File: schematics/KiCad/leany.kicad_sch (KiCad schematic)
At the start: 23 parts, among them J1 SWD, J2 SSD1306, SW2 ZERO_BTN, SW3 HOLD_BTN, SW4 BOOTMODE_SW, U1 STM32F103C8Tx, U3 LSM6DSO, U4 CH340C, Y1 8MHz

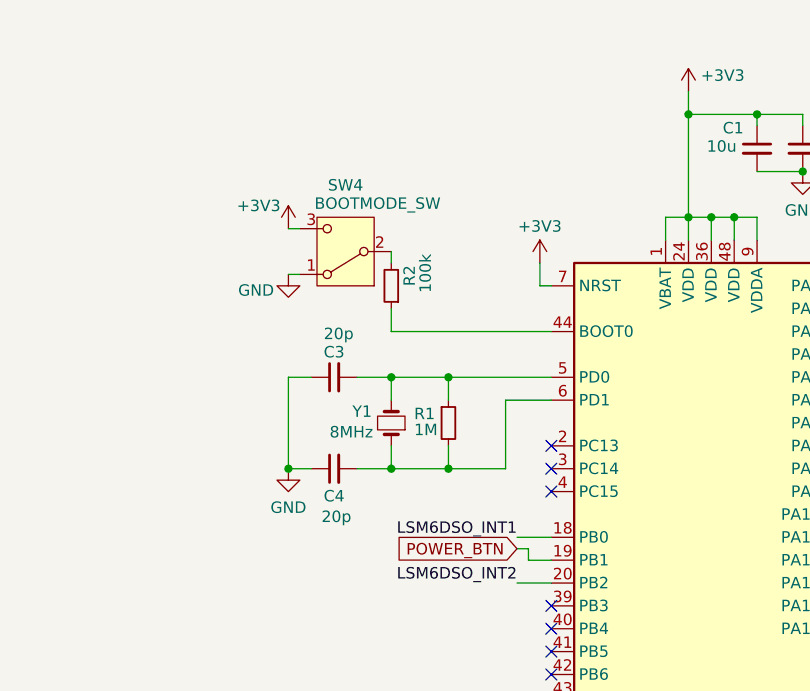
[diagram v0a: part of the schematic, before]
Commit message: wire up the charge controller
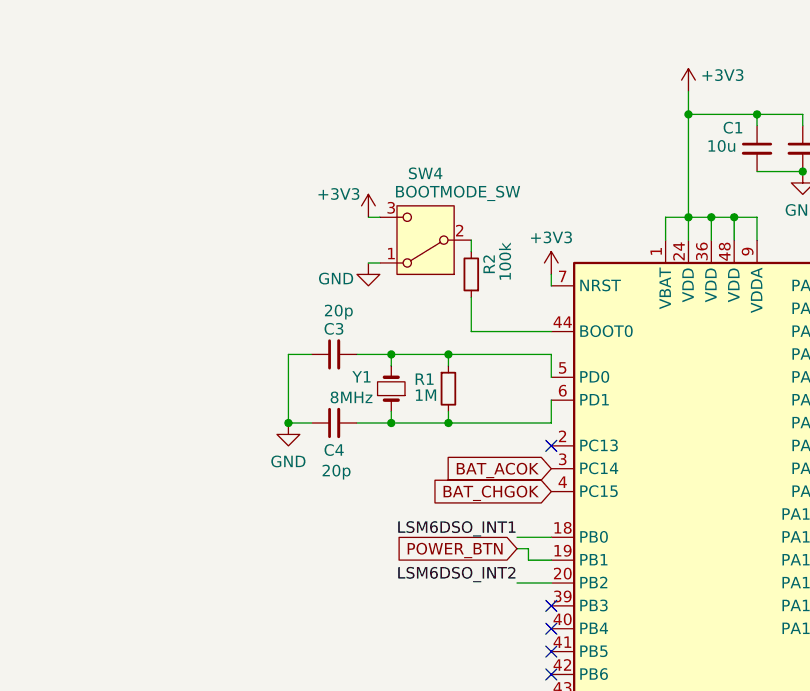
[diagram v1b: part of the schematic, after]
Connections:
- net BAT_ACOK: now reaches U1.3 (PC14)
- net BAT_CHGOK: now reaches U1.4 (PC15)
- no-connect marks 20 -> 18
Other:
- moved on the sheet: C3, C4, R1, R2, SW4, Y1

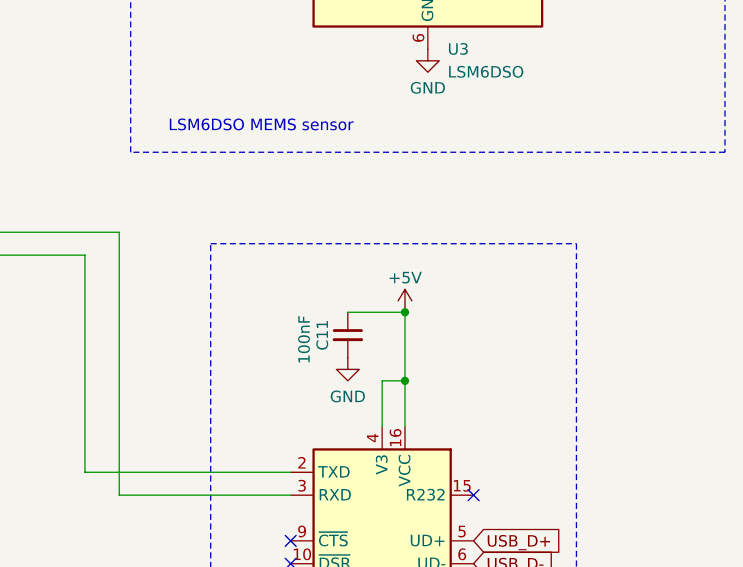
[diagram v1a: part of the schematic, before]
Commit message: indicate a direct wiring of USB output
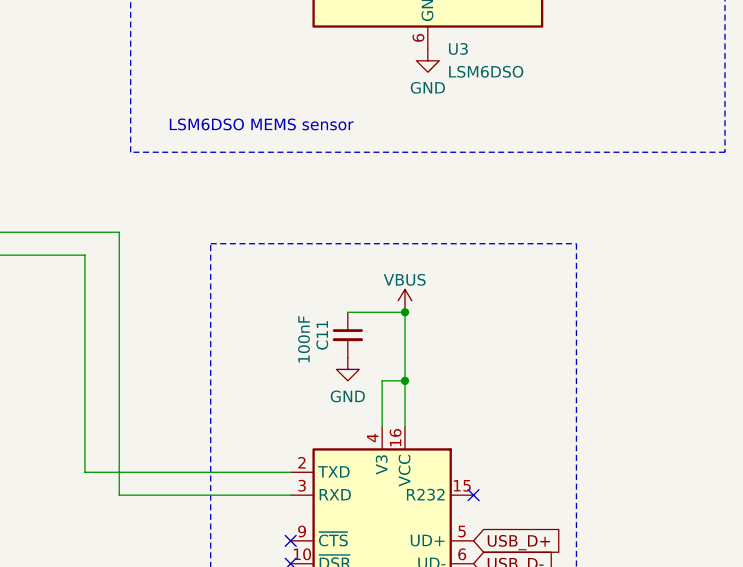
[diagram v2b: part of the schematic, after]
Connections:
- net +5V renamed VBUS
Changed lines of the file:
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@@
-	)
-	(junction
-		(at 228.6 100.33)
-		(diameter 0)
-		(color 0 0 0 0)
 	)
 	(junction
@@
 	(junction
 		(at 231.14 38.1)
+		(diameter 0)
+		(color 0 0 0 0)
+	)
+	(junction
+		(at 228.6 100.33)
 		(diameter 0)
 		(color 0 0 0 0)
@@
 	)
 	(symbol
-		(lib_id "power:+5V")
-		(at 228.6 100.33 0)
-		(mirror y)
-		(unit 1)
-		(exclude_from_sim no)
-		(in_bom yes)
-		(on_board yes)
-		(dnp no)
-		(property "Reference" "#PWR025"
-			(at 228.6 104.14 0)
-			(effects
-				(font
-					(size 1.27 1.27)
-				)
-				(hide yes)
-			)
-		)
-		(property "Value" "+5V"
-			(at 228.6 96.52 0)
-			(effects
-				(font
-					(size 1.27 1.27)
-				)
-			)
-		)
-		(property "Footprint" ""
-			(at 228.6 100.33 0)
-			(effects
-				(font
-					(size 1.27 1.27)
-				)
-				(hide yes)
-			)
-		)
-		(property "Datasheet" ""
-			(at 228.6 100.33 0)
-			(effects
-				(font
-					(size 1.27 1.27)
-				)
-				(hide yes)
-			)
-		)
-		(property "Description" "Power symbol creates a global label with name \"+5V\""
-			(at 228.6 100.33 0)
-			(effects
-				(font
-					(size 1.27 1.27)
-				)
-				(hide yes)
-			)
-		)
-		(pin "1"
-		)
-		(instances
-			(project "leany"
-				(path "/e47b2519-93ca-4a48-9414-ecc253dd35f5"
-					(reference "#PWR025")
-					(unit 1)
-				)
-			)
-		)
-	)
-	(symbol
 		(lib_id "power:GND")
 		(at 107.95 66.04 0)
@@
 					(unit 1)
 				)
+			)
+		)
+	)
+	(symbol
+		(lib_id "power:VBUS")
+		(at 228.6 100.33 0)
+		(unit 1)
+		(exclude_from_sim no)
+		(in_bom yes)
+		(on_board yes)
+		(dnp no)
+		(property "Reference" "#PWR032"
+			(at 228.6 104.14 0)
+			(effects
+				(font
+					(size 1.27 1.27)
+				)
+				(hide yes)
+			)
+		)
+		(property "Value" "VBUS"
+			(at 228.6 96.774 0)
+			(effects
+				(font
+					(size 1.27 1.27)
+				)
+			)
+		)
+		(property "Footprint" ""
+			(at 228.6 100.33 0)
+			(effects
+				(font
+					(size 1.27 1.27)
+				)
+				(hide yes)
+			)
+		)
+		(property "Datasheet" ""
+			(at 228.6 100.33 0)
+			(effects
+				(font
+					(size 1.27 1.27)
+				)
+				(hide yes)
+			)
+		)
+		(property "Description" "Power symbol creates a global label with name \"VBUS\""
+			(at 228.6 100.33 0)
+			(effects
+				(font
+					(size 1.27 1.27)
+				)
+				(hide yes)
+			)
+		)
+		(pin "1"
+		)
+		(instances
+			(project "leany"
+				(path "/e47b2519-93ca-4a48-9414-ecc253dd35f5"
+					(reference "#PWR032")
+					(unit 1)
+				)

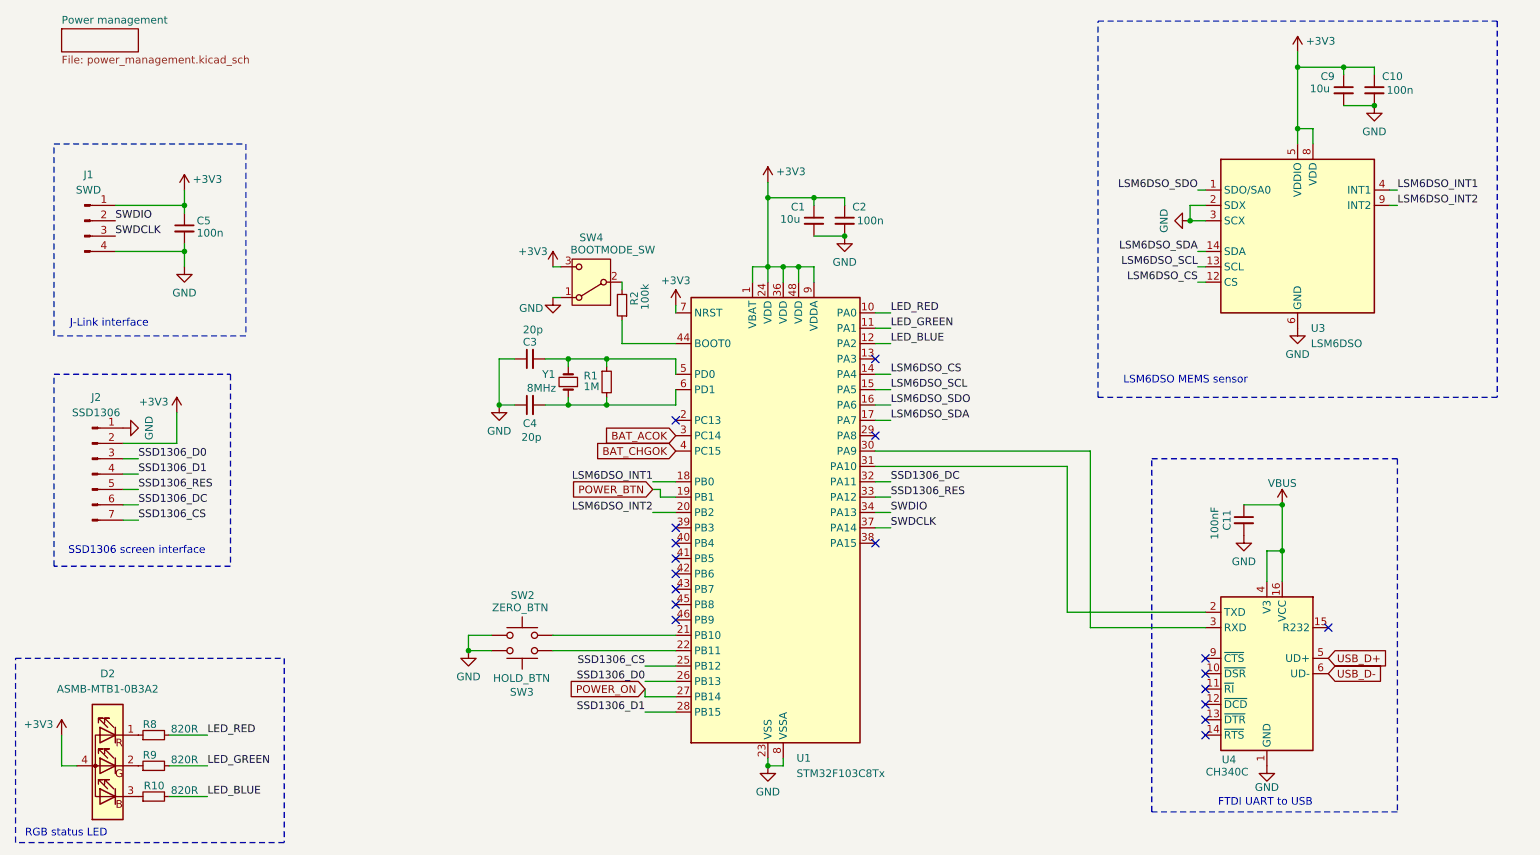
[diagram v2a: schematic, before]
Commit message: move bootmode switch near FTDI section
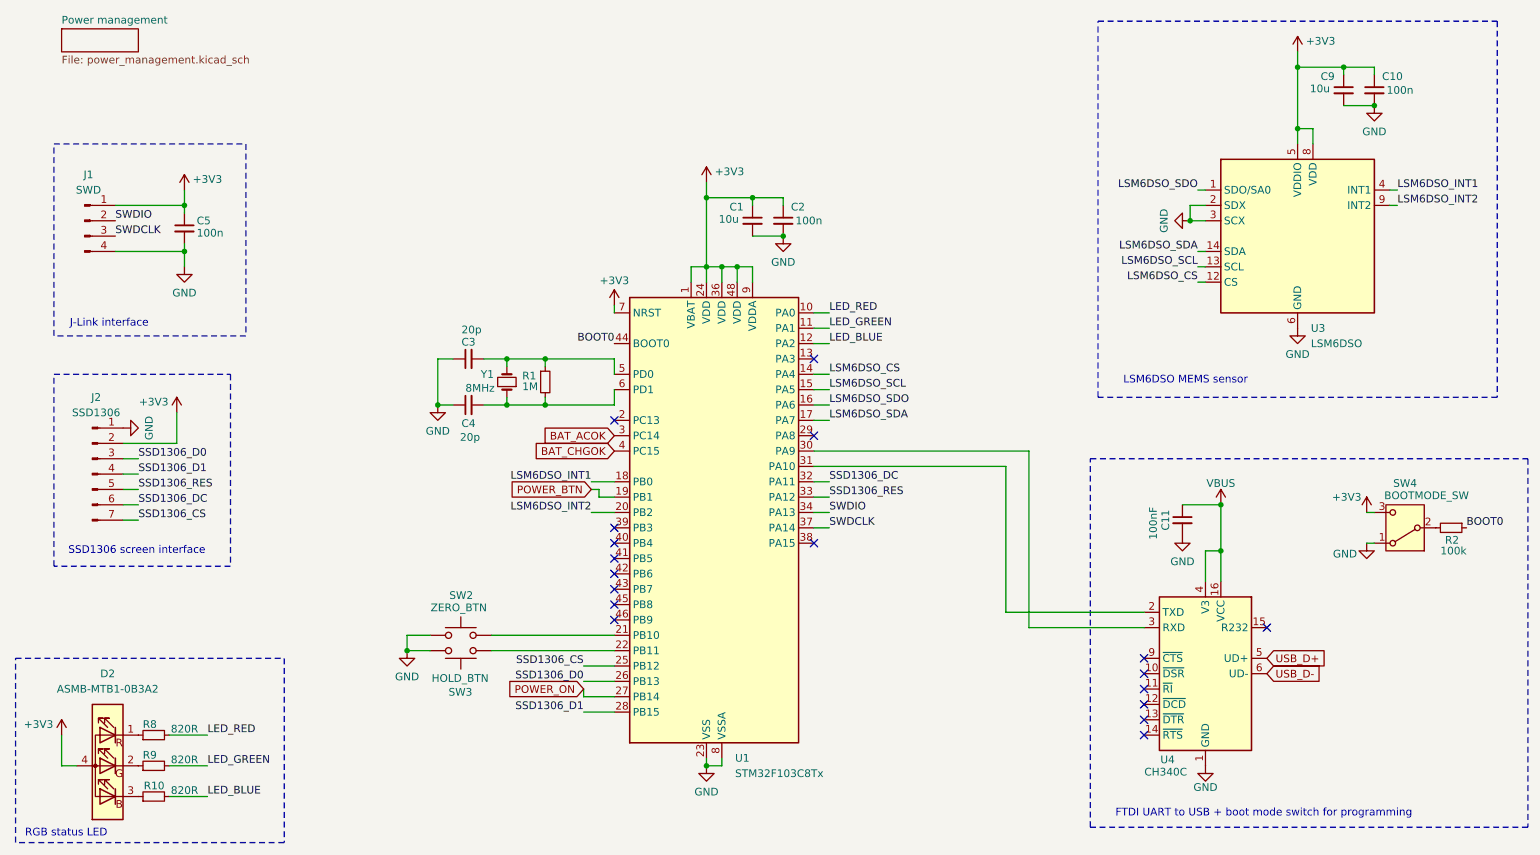
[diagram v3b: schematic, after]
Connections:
- net BOOT0: now reaches R2.1, U1.44 (BOOT0)
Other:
- note added: "FTDI UART to USB + boot mode switch for programming"
- note removed: "FTDI UART to USB"
- moved on the sheet: C1, C11, C2, C3, C4, R1, R2, SW2, SW3, SW4, U1, U4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

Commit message: clear annotations
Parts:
- renumbered C9 to C?, C1 to C?, C4 to C?, C5 to C?, C10 to C?, C2 to C?, C3 to C?, C11 to C?, D2 to D?, J1 to J?, J2 to J?, R10 to R?, R9 to R?, R2 to R?, R1 to R?, R8 to R?, SW4 to SW?, SW2 to SW?, SW3 to SW?, U1 to U?, U4 to U?, U3 to U?, Y1 to Y?

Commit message: re-annotate components
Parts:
- gave numbers to parts that had none: 23

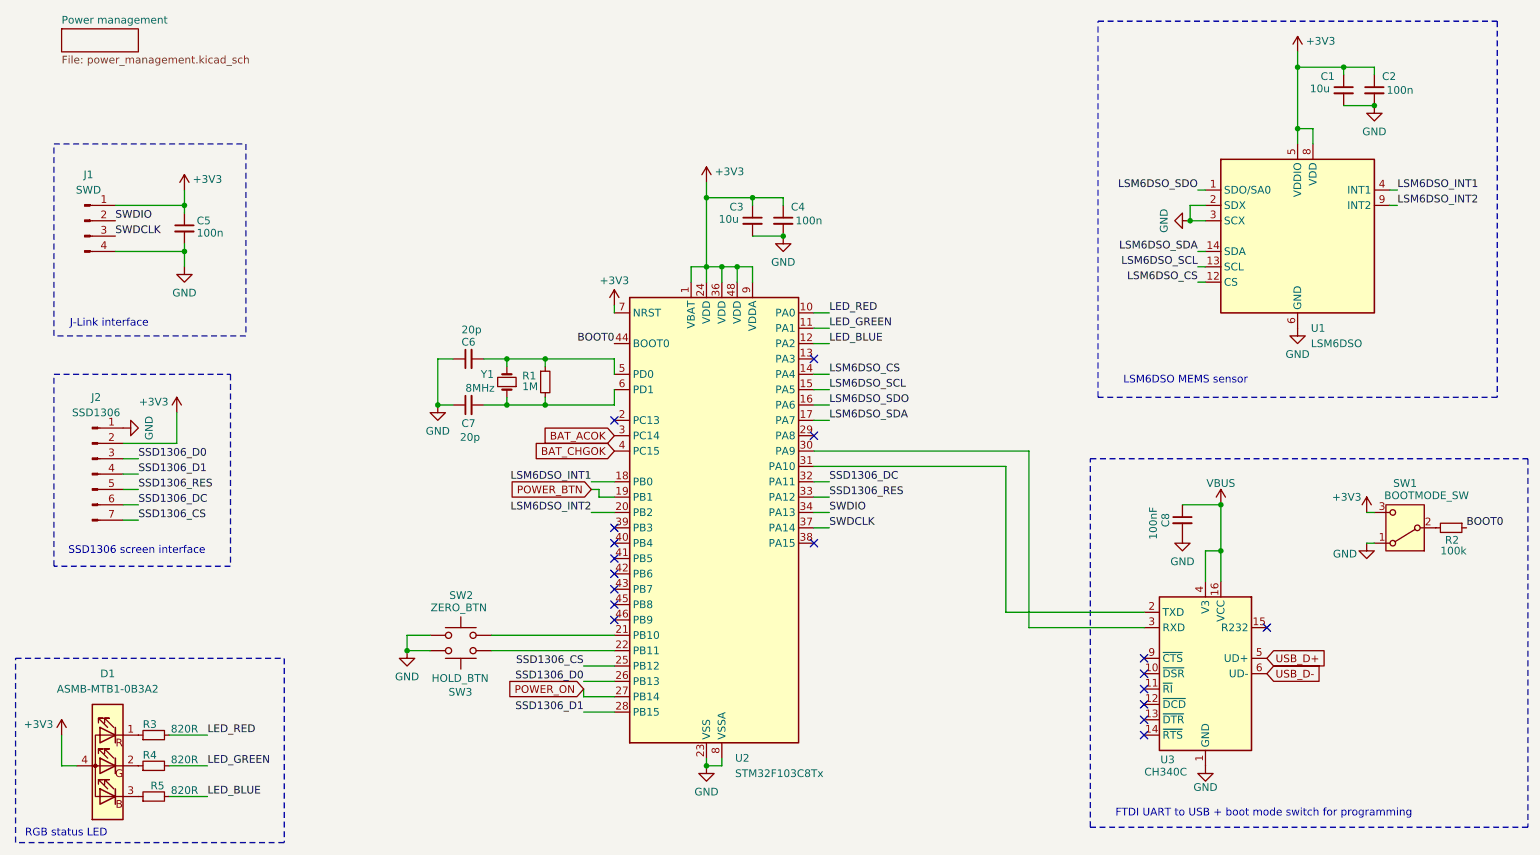
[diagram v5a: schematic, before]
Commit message: move MCU decoupling close to MCU
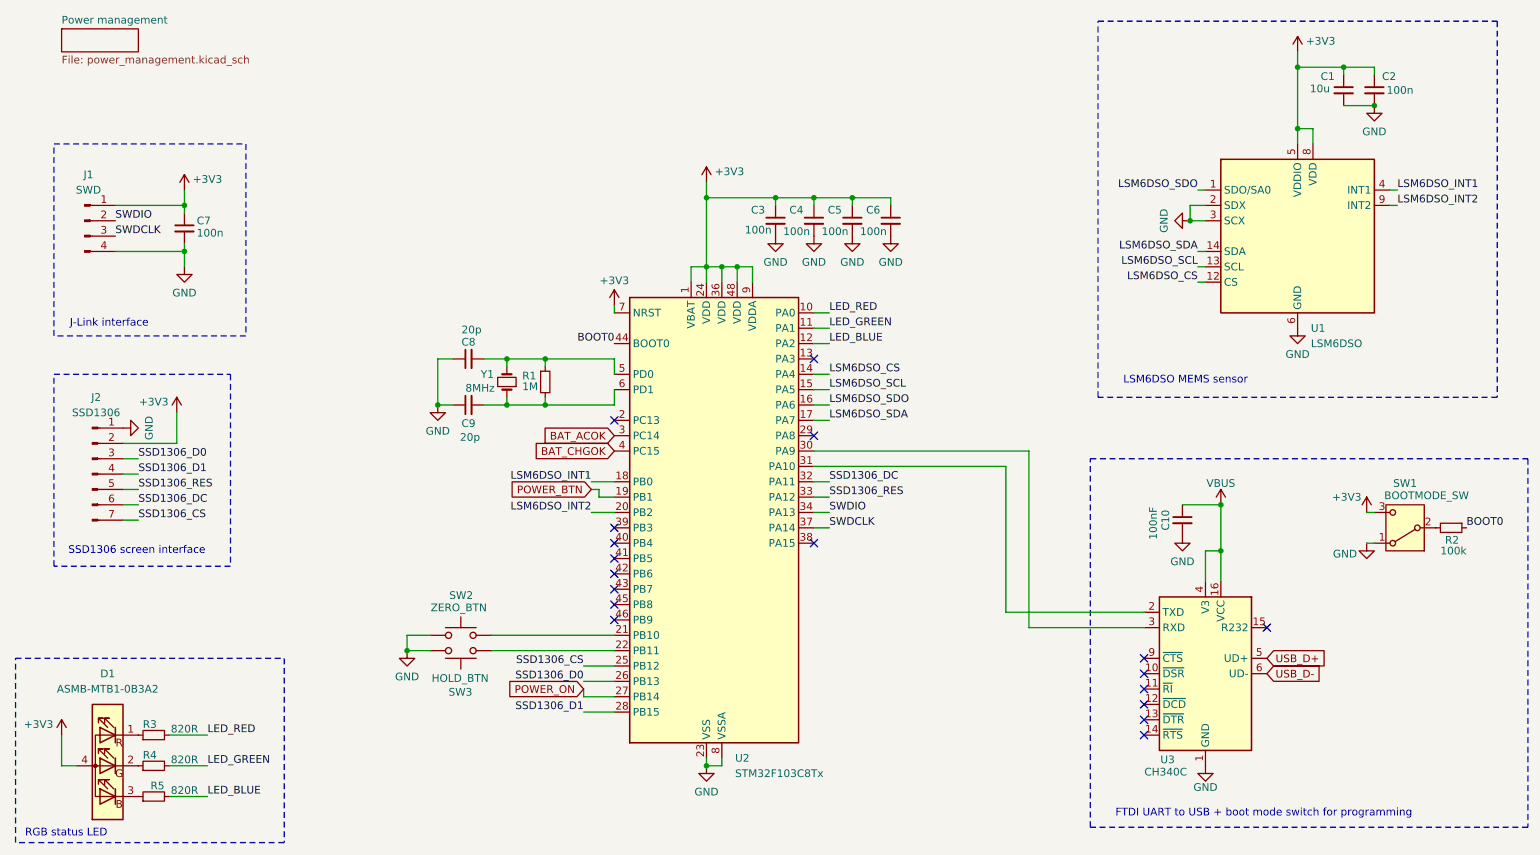
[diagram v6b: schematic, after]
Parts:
- added C5, C6: 100n, Capacitor_SMD:C_0201_0603Metric, symbol Device:C_Small
- C3: value 10u -> 100n
- renumbered C8 to C10, C5 to C7, C6 to C8, C7 to C9
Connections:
- net +3V3: now also C5.1, C6.1
- net GND: now also C5.2, C6.2
